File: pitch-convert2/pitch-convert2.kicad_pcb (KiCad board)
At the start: 2 copper layers, 10.6 x 41.1 mm, 4 parts, among them J1 Conn_01x16_Pin, J2 Conn_01x16_Pin, J3 Conn_01x16_Pin, J4 Conn_01x16_Pin

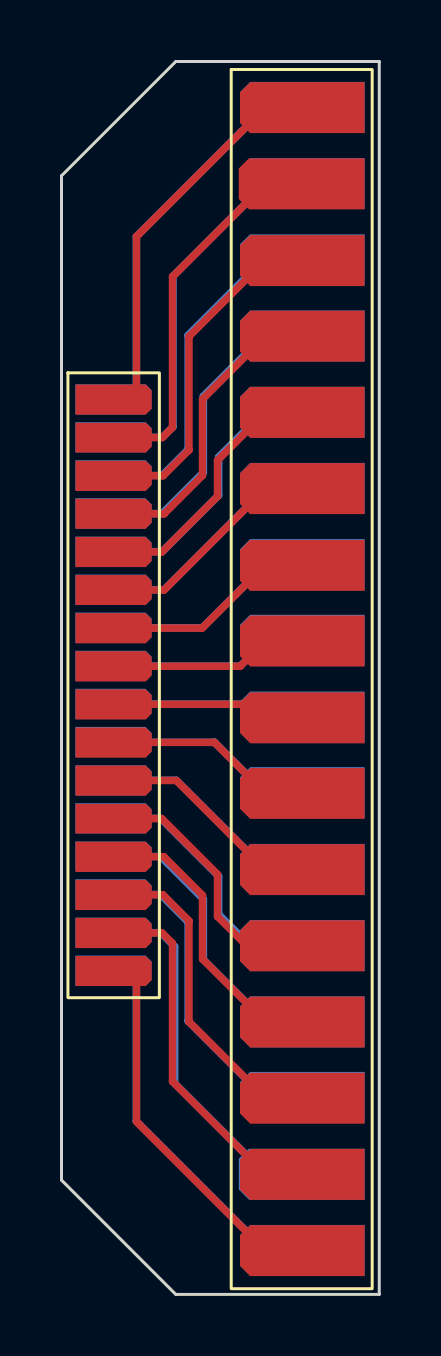
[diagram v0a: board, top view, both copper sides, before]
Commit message: 좌표 미세 조정
Signed-off-by: Ju, Gyeong-min <jcmh74@gmail.com>
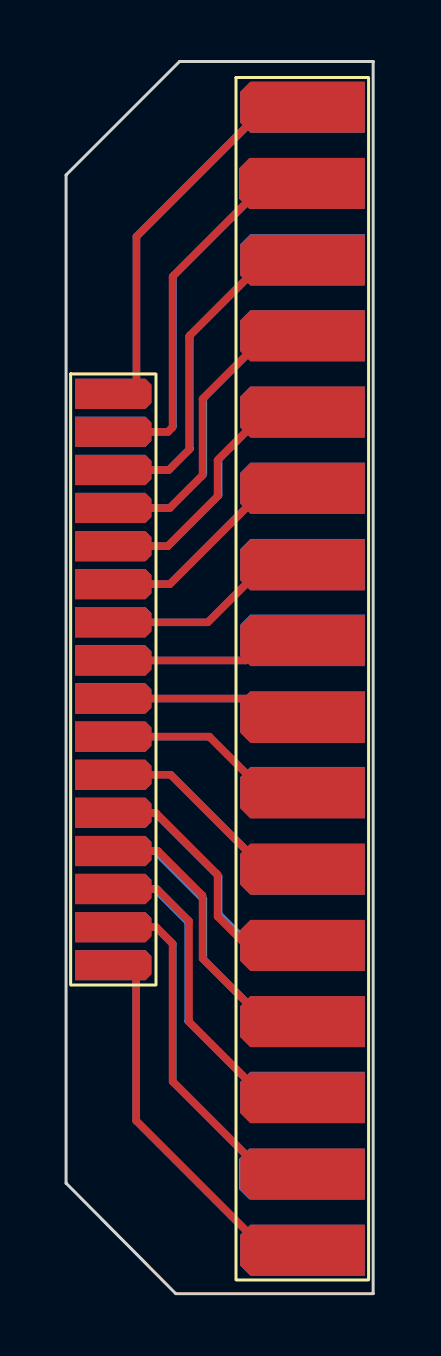
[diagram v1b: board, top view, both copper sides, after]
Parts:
- moved J2 0.19 mm to (139.6, 87.1)
- moved J4 0.18 mm to (139.6, 106.2)
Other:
- board size 10.6 x 41.1 mm -> 10.2 x 41.1 mm
